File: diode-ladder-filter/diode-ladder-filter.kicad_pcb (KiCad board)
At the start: 2 copper layers, 68 parts, among them J1 Input, J2 CV1, J3 CV2, J4 Output, J5 Power, J6 Power, J7 Power, SW1 LPF, SW2 Resonance_safety, SW3 BPF, SW4 HPF, U1 TL074, U2 TL074

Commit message: Update diode ladder
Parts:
- moved R23 234.8 mm to (239.3, 141.5)
- moved R20 219.7 mm to (225.7, 122.9)
- moved R21 219.7 mm to (225.7, 127.0)
- moved R11 218.4 mm to (231.8, 44.5)
- moved RV2 170.3 mm to (226.0, 64.5), turned to 90 degrees
- moved C8 164.4 mm to (244.9, 128.4)
- moved D1 162.9 mm to (247.9, 40.2)
- moved D2 162.9 mm to (247.9, 44.5)
- moved R10 159.2 mm to (264.1, 51.9)
- moved R9 159.2 mm to (269.1, 52.0)
- moved U2 156.2 mm to (225.4, 82.3)
- moved J4 152.6 mm to (265.0, 137.5)
- moved R14 150.1 mm to (136.3, 123.4)
- moved R15 150.1 mm to (136.3, 127.5)
- moved R16 150.1 mm to (136.3, 131.5)
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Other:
- board text added: "RES. MODE"
- board text added: "TAME"
- board text added: "WILD"

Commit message: Update diode ladder
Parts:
- moved G*** 176.9 mm to (249.5, 176.5)
- moved RV1 169.7 mm to (44.4, 187.5), turned to 90 degrees
- moved RV5 165.5 mm to (58.9, -3.50), turned to 90 degrees
- moved J1 159.0 mm to (26.9, 179.9)
- moved C1 148.7 mm to (39.0, 187.5), turned to 180 degrees
- moved R3 142.3 mm to (38.5, 185.0), turned to 90 degrees
- moved R1 135.8 mm to (45.8, 116.6)
- moved R2 135.8 mm to (45.8, 120.6)
- moved R4 135.8 mm to (45.8, 124.6)
- moved R7 135.8 mm to (45.8, 128.5)
- moved R8 135.8 mm to (45.8, 132.6)
- moved R5 134.5 mm to (35.0, 185.0), turned to 90 degrees
- moved J2 128.5 mm to (30.5, 30.0)
- moved C7 121.7 mm to (104.0, 36.5)
- moved D10 121.7 mm to (111.7, 41.0)
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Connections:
- C8 pad 2: Net-(U2D--) -> Net-(U2C--)
- R20 pad 1: Net-(U2B--) -> Net-(U2A--)
- R20 pad 2: Net-(U2C--) -> Net-(U2B--)
- R21 pad 1: Net-(U2D--) -> Net-(U2C--)
- R23 pad 1: Net-(U2D-+) -> Net-(U2C-+)
- RV2 pad 1: Net-(U2B--) -> Net-(U2A--)
- RV2 pad 2: Net-(U2A-+) -> Net-(U2D-+)
- RV7 pad 1: Net-(U2C--) -> Net-(U2B--)
- U2 pad 1: Net-(D1-A) -> Net-(U2A--)
- U2 pad 10: GND -> Net-(U2C-+)
- U2 pad 13: Net-(U2D--) -> Net-(D1-K)
- U2 pad 14: Net-(U2D--) -> Net-(D1-A)
- U2 pad 2: Net-(D1-K) -> Net-(U2A--)
- U2 pad 3: Net-(U2A-+) -> Net-(D5-K)
- U2 pad 5: Net-(D5-K) -> GND
- U2 pad 7: Net-(U2B--) -> Net-(C8-Pad1)
- U2 pad 8: Net-(C8-Pad1) -> Net-(U2C--)
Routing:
- net Net-(J1-Pin_1): track 0.00 -> 25.6 mm
- net GND: track 0.00 -> 24.3 mm
- net Net-(U1B-+): track 0.00 -> 15.1 mm
- net Net-(C1-Pad1): track 0.00 -> 8.89 mm
- net Net-(C1-Pad2): track 0.00 -> 6.41 mm
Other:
- board text added: "0"
- board text added: "1"
- board text added: "CUTOFF"
- board text added: "CV1"
- board text added: "CV2"
- board text added: "FILTER TYPE"
- board text added: "INPUT"
- board text added: "OUTPUT"
- board text added: "SOFT ENV."
- board text added: "VOLUME"
- board text removed: "RES. MODE"

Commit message: Update some modules
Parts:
- added F1: foot, modular2:foot, B.Cu at (66.1, 36.1)
- added F2: foot, modular2:foot, B.Cu at (137.9, 36.1)
- added F3: foot, modular2:foot, B.Cu at (66.1, 165.9)
- added F4: foot, modular2:foot, B.Cu at (137.9, 165.9)
- added G***: LOGO, modular2:ibis-small, F.Cu at (215.0, 137.5)
- added H1: MountingHole_3.2mm_M3, MountingHole:MountingHole_3.2mm_M3, F.Cu at (189.5, 32.0)
- added H1: MountingHole_3.2mm_M3, MountingHole:MountingHole_3.2mm_M3, F.Cu at (76.5, 47.0)
- added H2: MountingHole_3.2mm_M3, MountingHole:MountingHole_3.2mm_M3, F.Cu at (240.5, 32.0)
- added H2: MountingHole_3.2mm_M3, MountingHole:MountingHole_3.2mm_M3, F.Cu at (127.5, 47.0)
- added H3: MountingHole_3.2mm_M3, MountingHole:MountingHole_3.2mm_M3, F.Cu at (189.5, 154.0)
- added H3: MountingHole_3.2mm_M3, MountingHole:MountingHole_3.2mm_M3, F.Cu at (76.5, 169.0)
- added H4: MountingHole_3.2mm_M3, MountingHole:MountingHole_3.2mm_M3, F.Cu at (127.5, 169.0)
- added H4: MountingHole_3.2mm_M3, MountingHole:MountingHole_3.2mm_M3, F.Cu at (240.5, 154.0)
- added J10: Input, modular2:banana-jack, F.Cu at (182.3, 137.8)
- added J11: Output, modular2:banana-jack, F.Cu at (248.0, 137.7)
- added J12: Conn_01x04_Socket, Connector_PinSocket_2.54mm:PinSocket_1x04_P2.54mm_Vertical, F.Cu at (72.2, 57.5)
- added J13: Conn_01x04_Pin, Connector_PinHeader_2.54mm:PinHeader_1x04_P2.54mm_Vertical, B.Cu at (185.2, 42.5)
- added J8: CV1, modular2:banana-jack, F.Cu at (182.4, 62.4)
- added J9: CV2, modular2:banana-jack, F.Cu at (182.4, 86.5)
- moved G*** 149.7 mm to (101.5, 154.0)
- moved R9 104.5 mm to (127.1, 78.0), turned to 90 degrees
- moved R10 102.6 mm to (124.1, 78.0), turned to 90 degrees
- moved D1 95.9 mm to (124.2, 87.8), turned to 90 degrees
- moved R22 92.5 mm to (90.2, 117.2)
- moved D9 90.5 mm to (71.7, 117.9), turned to 180 degrees
- moved D2 84.5 mm to (130.0, 80.1), turned to -90 degrees
- moved J4 79.0 mm to (135.0, 152.7)
- moved R20 79.0 mm to (125.6, 150.2)
- moved R21 79.0 mm to (130.2, 144.8)
- moved RV7 79.0 mm to (112.6, 160.3)
- moved C8 79.0 mm to (122.7, 144.8)
- moved RV5 78.7 mm to (99.4, 64.0)
- moved C7 77.2 mm to (113.1, 113.2)
- moved RV2 76.5 mm to (113.1, 85.8)
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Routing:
- net GND: track 24.3 -> 370.2 mm
- net -12V: track 0.00 -> 219.1 mm
- net 12V: track 0.00 -> 213.1 mm
- net Net-(J12-Pin_4): track 0.00 -> 148.0 mm
- net Net-(D10-A): track 0.00 -> 121.6 mm
- net Net-(J11-Pin_1): track 0.00 -> 118.1 mm
- net Net-(J1-Pin_1): track 25.6 -> 132.1 mm
- net Net-(J10-Pin_1): track 0.00 -> 98.7 mm
- net Net-(J12-Pin_2): track 0.00 -> 72.6 mm
- net Net-(U2A--): track 0.00 -> 69.6 mm
- net Net-(D3-A): track 0.00 -> 69.2 mm
- net Net-(D1-A): track 0.00 -> 68.9 mm
- net Net-(D1-K): track 0.00 -> 59.1 mm
- net Net-(SW1A-A): track 0.00 -> 58.1 mm
- net Net-(SW3A-B): track 0.00 -> 57.1 mm
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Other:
- board outline added: 198 x 145.1 mm
- board text added: "SCALE"

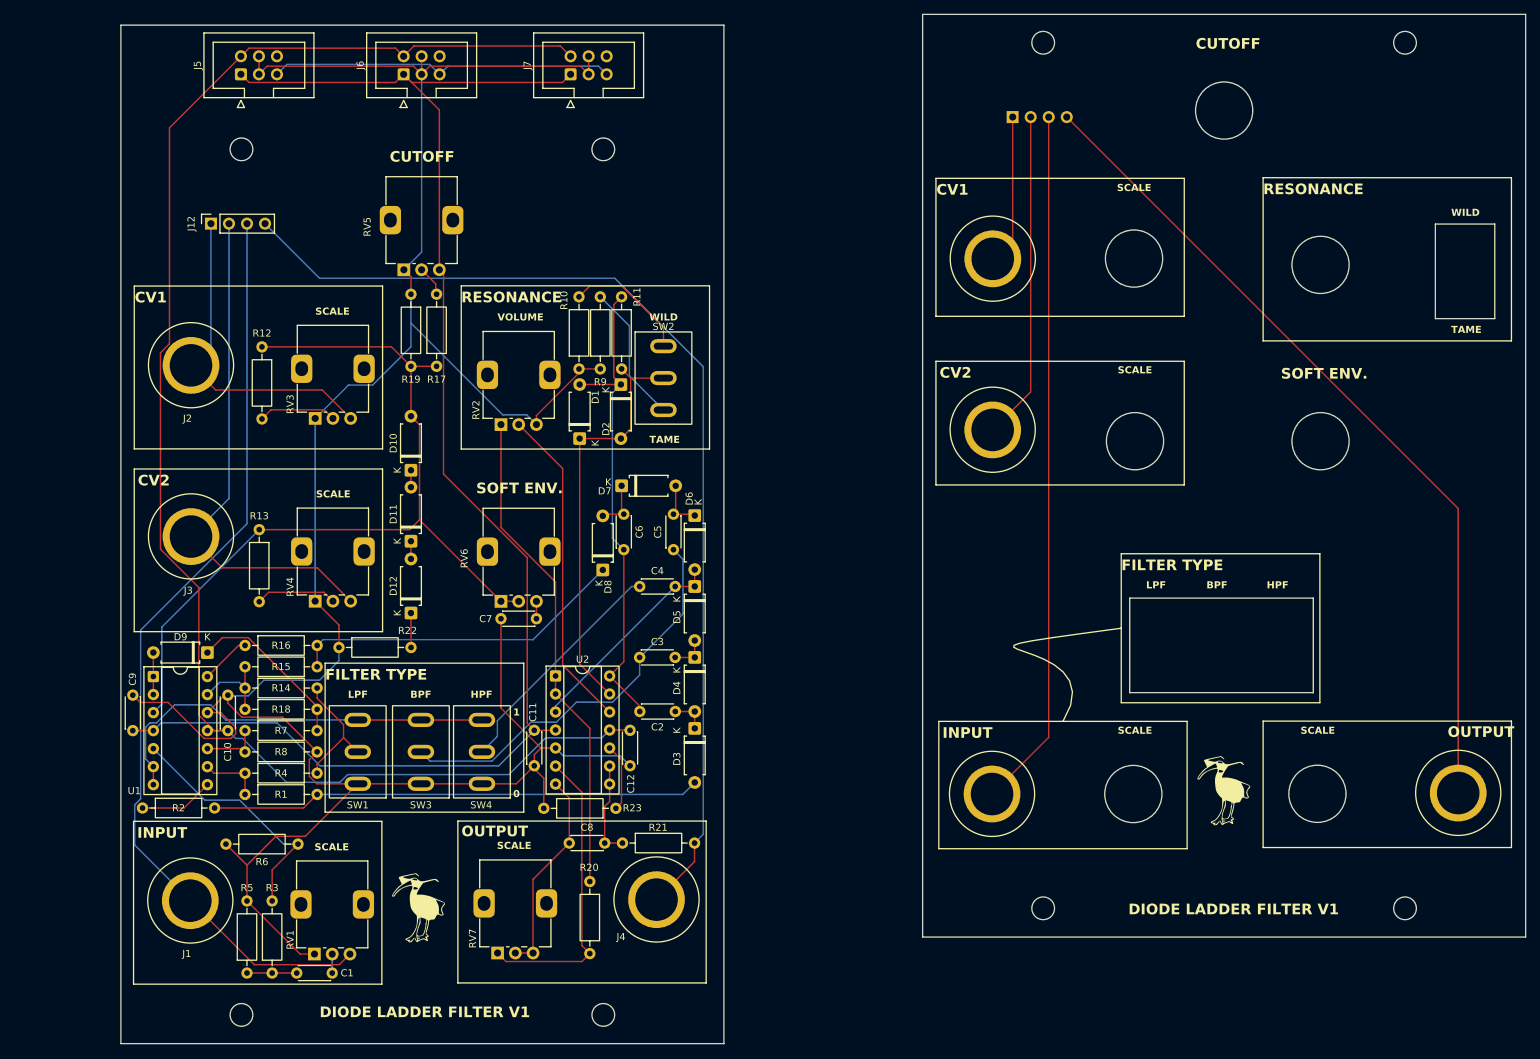
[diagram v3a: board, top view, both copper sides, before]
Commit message: Start fixing issues with diode ladder
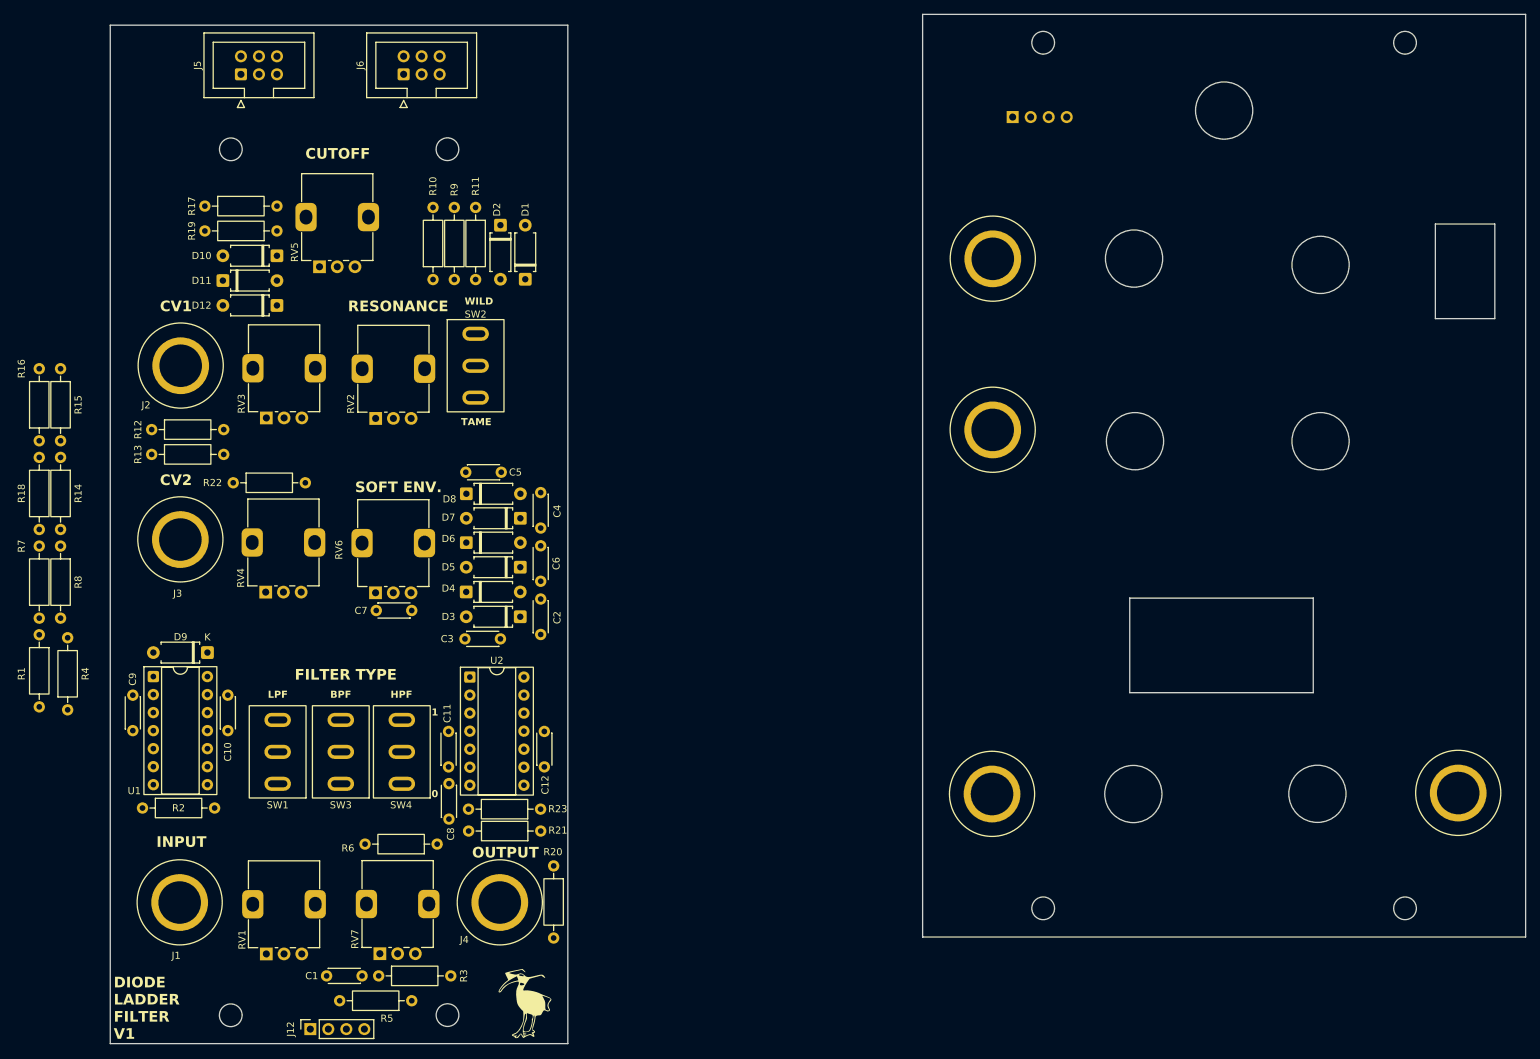
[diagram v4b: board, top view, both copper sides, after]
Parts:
- removed the G*** at (215.0, 137.5)
- removed J7: Power, Connector_IDC:IDC-Header_2x03_P2.54mm_Vertical
- R20: value 100 -> 1K
- moved J12 114.4 mm to (86.2, 171.0)
- moved R15 55.4 mm to (51.0, 77.9), turned to -90 degrees
- moved D12 47.3 mm to (81.5, 69.0), turned to 180 degrees
- moved R8 46.4 mm to (51.0, 102.9), turned to -90 degrees
- moved R18 45.8 mm to (48.0, 90.4), turned to -90 degrees
- moved D11 45.3 mm to (73.9, 65.5), turned to 0 degrees
- moved R14 41.6 mm to (51.0, 90.4), turned to -90 degrees
- moved R16 40.9 mm to (48.0, 88.1), turned to 90 degrees
- moved R17 39.7 mm to (71.3, 55.0), turned to 0 degrees
- moved R1 36.7 mm to (48.0, 115.4), turned to -90 degrees
- moved R4 36.3 mm to (52.0, 126.0), turned to 90 degrees
- moved D10 35.7 mm to (81.5, 62.0), turned to 180 degrees
- moved D4 33.5 mm to (108.2, 109.4), turned to 0 degrees
- moved R7 33.0 mm to (48.0, 113.1), turned to 90 degrees
- moved D6 32.4 mm to (108.2, 102.4), turned to 0 degrees
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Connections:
- C8 pad 2: Net-(U2C--) -> Net-(U2C-+)
- RV2 pad 1: Net-(U2A--) -> GND
- RV2 pad 3: GND -> Net-(U2A--)
- SW1 pad 1: Net-(SW1A-A) -> GND
- SW1 pad 3: GND -> Net-(SW1A-C)
- SW3 pad 1: Net-(SW1A-A) -> GND
- SW3 pad 3: GND -> Net-(SW1A-C)
- SW4 pad 1: Net-(SW1A-A) -> GND
- SW4 pad 3: GND -> Net-(SW1A-C)
- U1 pad 6: Net-(SW1A-A) -> Net-(SW1A-C)
- U1 pad 7: Net-(SW1A-A) -> Net-(SW1A-C)
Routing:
- net GND: track 370.2 -> 0.00 mm
- net -12V: track 219.1 -> 0.00 mm
- net 12V: track 213.1 -> 0.00 mm
- net Net-(J12-Pin_4): track 148.0 -> 0.00 mm
- net Net-(J1-Pin_1): track 132.1 -> 0.00 mm
- net Net-(D10-A): track 121.6 -> 0.00 mm
- net Net-(J11-Pin_1): track 118.1 -> 0.00 mm
- net Net-(J10-Pin_1): track 98.7 -> 0.00 mm
- net Net-(J12-Pin_2): track 72.6 -> 0.00 mm
- net Net-(U2A--): track 69.6 -> 0.00 mm
- net Net-(D3-A): track 69.2 -> 0.00 mm
- net Net-(D1-A): track 68.9 -> 0.00 mm
- net Net-(D1-K): track 59.1 -> 0.00 mm
- net Net-(SW1A-A): track 58.1 -> 0.00 mm
- net Net-(SW3A-B): track 57.1 -> 0.00 mm
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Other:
- board size 198 x 145.1 mm -> 199.5 x 145.1 mm
- board text removed: "SCALE"
- board text removed: "VOLUME"

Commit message: Diode ladder fixes and relayout
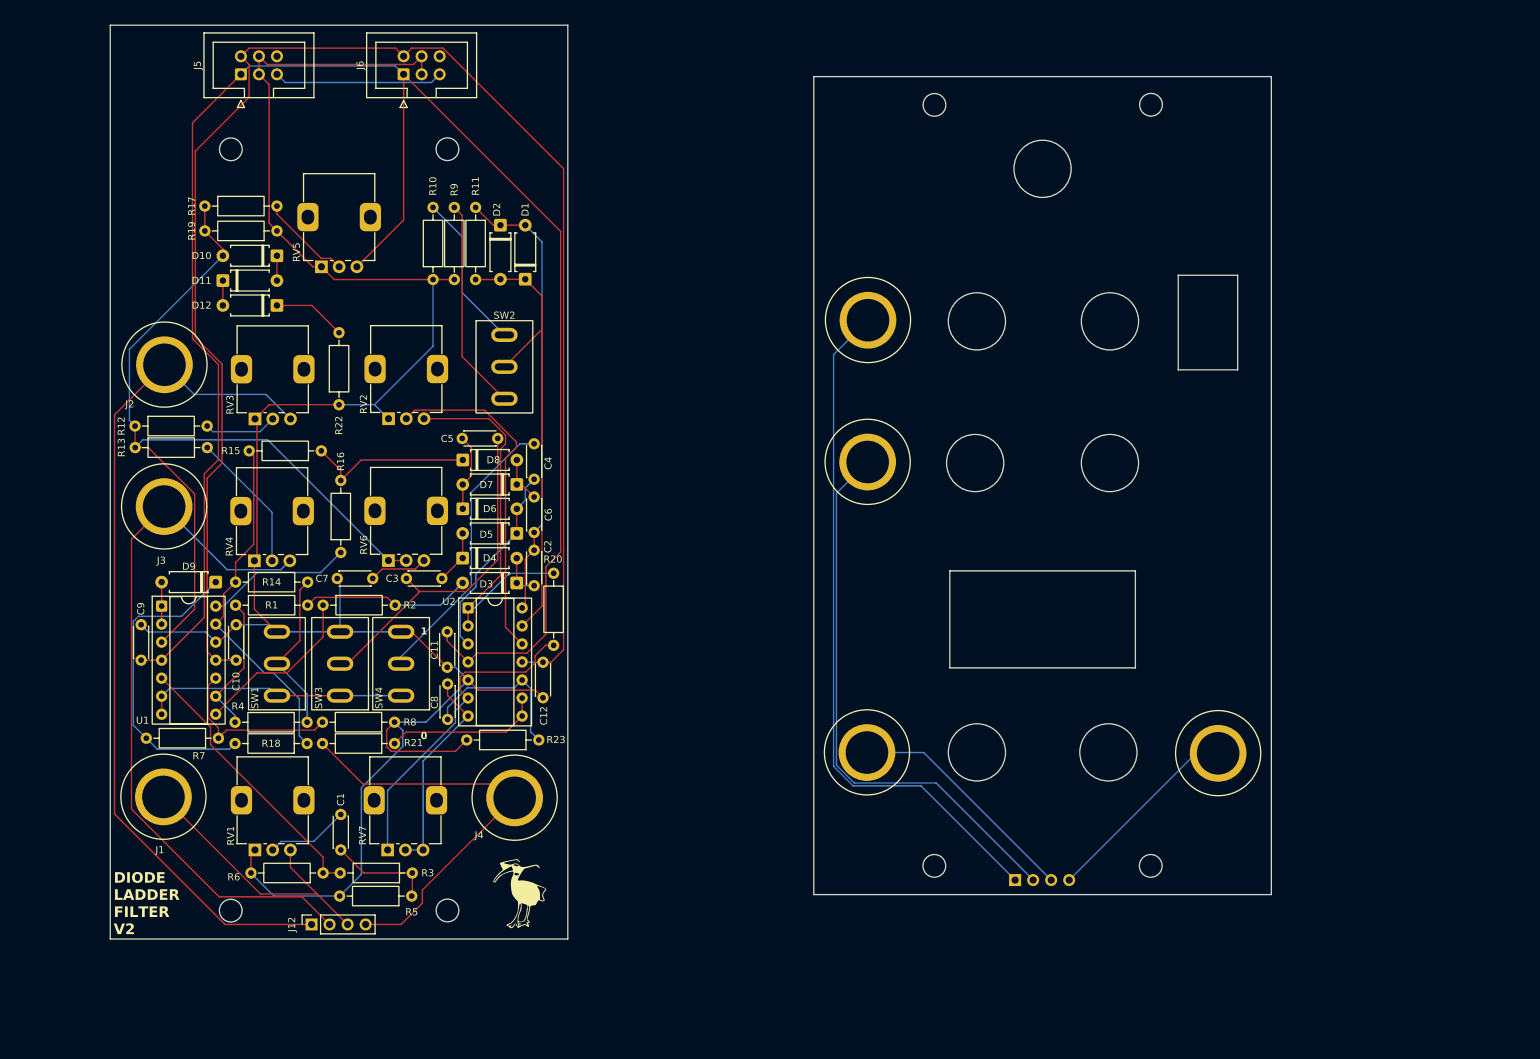
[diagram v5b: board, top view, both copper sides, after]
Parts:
- moved J13 107.5 mm to (185.5, 150.0)
- moved R18 55.2 mm to (85.8, 130.8), turned to 180 degrees
- moved R8 53.2 mm to (98.1, 127.7), turned to 180 degrees
- moved R16 45.3 mm to (90.5, 103.8)
- moved R20 41.2 mm to (120.5, 106.8)
- moved R15 38.5 mm to (87.8, 89.5), turned to 180 degrees
- moved R2 38.3 mm to (88.0, 111.2)
- moved H2 36.9 mm to (204.7, 40.7)
- moved H4 36.3 mm to (204.7, 148.0)
- moved J11 34.3 mm to (214.2, 132.1)
- moved R4 33.8 mm to (85.8, 127.8), turned to 180 degrees
- moved R7 30.4 mm to (73.2, 130.0), turned to 180 degrees
- moved R14 30.3 mm to (75.7, 108.0), turned to 0 degrees
- moved R1 28.0 mm to (75.7, 111.2), turned to 0 degrees
- moved R21 24.0 mm to (98.1, 130.8)
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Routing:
- net GND: track 0.00 -> 300.1 mm
- net 12V: track 0.00 -> 253.9 mm
- net -12V: track 0.00 -> 222.9 mm
- net Net-(J12-Pin_1): track 0.00 -> 121.4 mm
- net Net-(D10-A): track 0.00 -> 120.5 mm
- net Net-(J12-Pin_2): track 0.00 -> 101.1 mm
- net Net-(J13-Pin_1): track 0.00 -> 97.1 mm
- net Net-(J13-Pin_2): track 0.00 -> 79.0 mm
- net Net-(D1-K): track 0.00 -> 65.5 mm
- net Net-(D1-A): track 0.00 -> 64.7 mm
- net Net-(J12-Pin_4): track 0.00 -> 59.7 mm
- net Net-(U2A--): track 0.00 -> 55.6 mm
- net Net-(U1D--): track 0.00 -> 49.8 mm
- net Net-(SW3A-B): track 0.00 -> 49.1 mm
- net Net-(U2D-+): track 0.00 -> 47.9 mm
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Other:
- board size 199.5 x 145.1 mm -> 163.7 x 128.8 mm
- board text added: "DIODE LADDER FILTER V2"
- board text removed: "BPF"
- board text removed: "CUTOFF"
- board text removed: "CV1"
- board text removed: "CV2"
- board text removed: "DIODE LADDER FILTER V1"
- board text removed: "FILTER TYPE"
- board text removed: "HPF"
- board text removed: "INPUT"
- board text removed: "LPF"
- board text removed: "OUTPUT"
- board text removed: "RESONANCE"
- board text removed: "SOFT ENV."
- board text removed: "TAME"
- board text removed: "WILD"

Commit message: Renumber some components
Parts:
- moved H5 177.3 mm to (74.8, 187.6)
- moved H7 177.3 mm to (74.8, 294.9)
- moved H8 177.3 mm to (105.3, 294.9)
- moved J10 177.3 mm to (65.3, 278.9)
- moved J9 177.3 mm to (65.4, 237.9)
- moved H6 177.3 mm to (105.3, 187.6)
- moved J11 177.3 mm to (114.8, 279.0)
- moved J12 177.3 mm to (86.2, 296.9)
- moved J8 177.3 mm to (65.4, 217.9)
- renumbered C5 to C1, C11 to C10, C12 to C11, C1 to C12, C4 to C2, C9 to C3, C10 to C4, C7 to C5, C3 to C6, C6 to C7, C2 to C8, C8 to C9, D10 to D1, D7 to D10, D3 to D11, D5 to D12, D11 to D3, D12 to D4, D1 to D5, D9 to D6, D4 to D7, D6 to D8, D8 to D9, F2 to F0, F4 to F2, H1 to H5, H2 to H6, H3 to H7, H4 to H8, J5 to J1, J13 to J12, J6 to J2, J2 to J3, J3 to J4, J1 to J5, J4 to J6, J12 to J7, R19 to R1, R14 to R10, R2 to R11, R15 to R12, R16 to R13, R20 to R14, R7 to R15, R4 to R16, R18 to R17, R8 to R18, R21 to R19, R17 to R2, R23 to R20, R6 to R21, R3 to R22, R5 to R23, R11 to R3, R12 to R4, R9 to R5, R22 to R6, R10 to R7, R13 to R8, R1 to R9, RV5 to RV1, RV3 to RV2, RV2 to RV3, RV6 to RV5, RV1 to RV6, SW2 to SW1, SW1 to SW2
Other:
- board size 163.7 x 128.8 mm -> 64.7 x 269.4 mm

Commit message: Revert "Renumber some components"
This reverts commit 4c9a93e4336de2276d9b49e02718b6a92f997a6a.
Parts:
- moved H1 177.3 mm to (174.2, 40.7)
- moved H3 177.3 mm to (174.2, 148.0)
- moved H4 177.3 mm to (204.7, 148.0)
- moved J10 177.3 mm to (164.7, 132.0)
- moved J9 177.3 mm to (164.8, 91.0)
- moved H2 177.3 mm to (204.7, 40.7)
- moved J11 177.3 mm to (214.2, 132.1)
- moved J13 177.3 mm to (185.5, 150.0)
- moved J8 177.3 mm to (164.8, 71.1)
- renumbered C12 to C1, C4 to C10, C10 to C11, C11 to C12, C8 to C2, C6 to C3, C2 to C4, C1 to C5, C7 to C6, C5 to C7, C9 to C8, C3 to C9, D5 to D1, D1 to D10, D3 to D11, D4 to D12, D11 to D3, D7 to D4, D12 to D5, D8 to D6, D10 to D7, D9 to D8, D6 to D9, F0 to F2, F2 to F4, H5 to H1, H6 to H2, H7 to H3, H8 to H4, J5 to J1, J7 to J12, J12 to J13, J3 to J2, J4 to J3, J6 to J4, J1 to J5, J2 to J6, R9 to R1, R7 to R10, R3 to R11, R4 to R12, R8 to R13, R10 to R14, R12 to R15, R13 to R16, R2 to R17, R17 to R18, R1 to R19, R11 to R2, R14 to R20, R19 to R21, R6 to R22, R20 to R23, R22 to R3, R16 to R4, R23 to R5, R21 to R6, R15 to R7, R18 to R8, R5 to R9, RV6 to RV1, RV3 to RV2, RV2 to RV3, RV1 to RV5, RV5 to RV6, SW2 to SW1, SW1 to SW2
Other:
- board size 64.7 x 269.4 mm -> 163.7 x 128.8 mm

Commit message: Renumber some components
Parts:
- moved H5 166.7 mm to (74.6, 174.4)
- moved H6 166.7 mm to (105.1, 174.4)
- moved J9 166.7 mm to (65.2, 224.7)
- moved H7 166.7 mm to (74.6, 281.7)
- moved H8 166.7 mm to (105.1, 281.7)
- moved J10 166.7 mm to (65.1, 265.7)
- moved J11 166.7 mm to (114.6, 265.8)
- moved J12 166.7 mm to (85.9, 283.7)
- moved J8 166.7 mm to (65.2, 204.7)
- renumbered C5 to C1, C8 to C10, C12 to C11, C1 to C12, C4 to C2, C9 to C3, C10 to C4, C7 to C5, C3 to C6, C6 to C7, C2 to C8, C11 to C9, D10 to D1, D5 to D10, D3 to D11, D7 to D12, D12 to D3, D11 to D4, D1 to D5, D9 to D6, D6 to D7, D4 to D9, F2 to F0, F4 to F2, H1 to H5, H2 to H6, H3 to H7, H4 to H8, J5 to J1, J13 to J12, J6 to J2, J2 to J3, J3 to J4, J1 to J5, J4 to J6, J12 to J7, R17 to R1, R1 to R10, R2 to R11, R14 to R12, R16 to R13, R20 to R14, R18 to R15, R7 to R16, R4 to R17, R8 to R18, R21 to R19, R19 to R2, R23 to R20, R6 to R21, R5 to R22, R3 to R23, R11 to R3, R12 to R4, R22 to R5, R10 to R6, R9 to R7, R13 to R8, R15 to R9, RV5 to RV1, RV3 to RV2, RV2 to RV3, RV6 to RV5, RV1 to RV6, SW2 to SW1, SW1 to SW2, SW4 to SW3, SW3 to SW4
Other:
- board size 163.7 x 128.8 mm -> 64.9 x 256.2 mm
- board text removed: "0"
- board text removed: "1"
